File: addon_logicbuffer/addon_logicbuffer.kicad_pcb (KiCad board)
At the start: 2 copper layers, 24.4 x 17.3 mm, 8 parts, among them U1 SN74LVC1G07DBVR

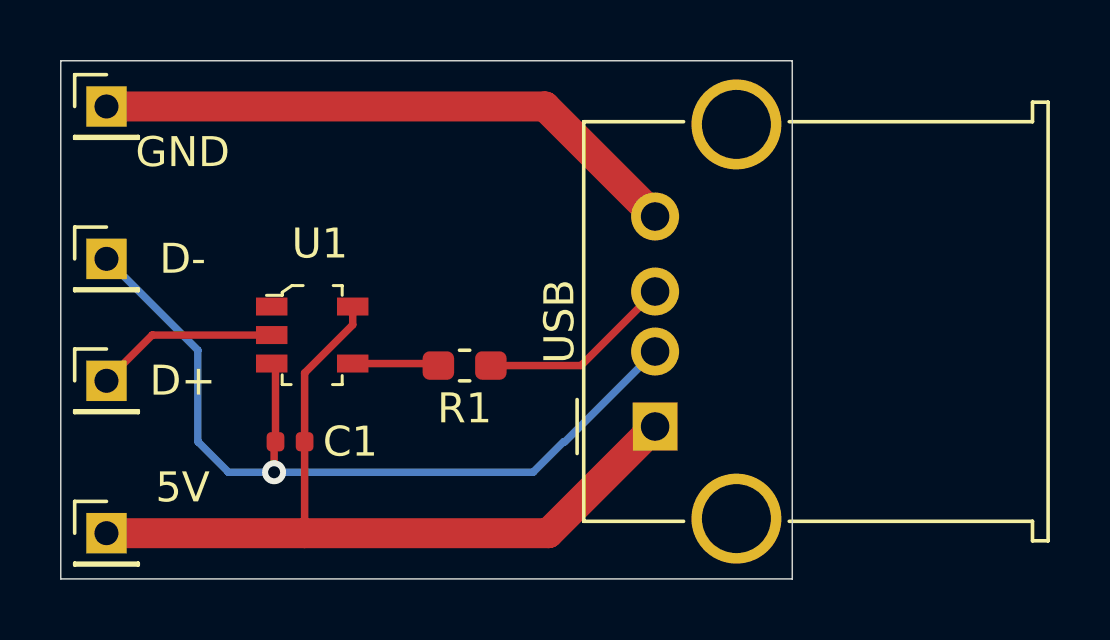
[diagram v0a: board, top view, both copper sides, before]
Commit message: update to kicad7
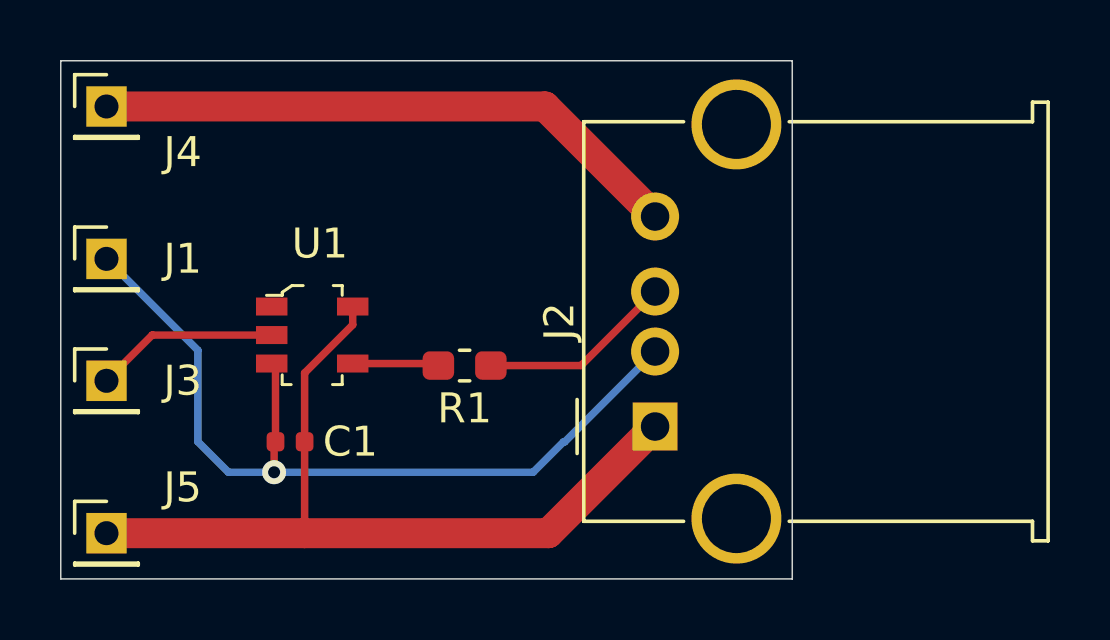
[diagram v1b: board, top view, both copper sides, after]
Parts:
- renumbered D- to J1, USB to J2, D+ to J3, GND to J4, 5V to J5
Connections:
- J2 pad 5: Net-(J2-Pad5) -> unconnected-(J2-Shield-Pad5)
- U1 pad 1: (no net) -> unconnected-(U1-NC-Pad1)
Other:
- net class Default removed
